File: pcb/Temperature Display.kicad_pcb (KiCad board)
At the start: 2 copper layers, 25.7 x 34.4 mm, 18 parts, among them P1 Connector_Generic:Conn_01x08, P2 Connector_Generic:Conn_01x08

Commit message: PCB cleanup / optimization and silkscreen adjustments
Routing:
- net /+3.3V: track 6.13 -> 0.00 mm
- net D2: vias 2 -> 0
- added copper zone on B.Cu, net /+3.3V
- added copper zone on F.Cu, net /GND
- removed copper zone on F.Cu, net /+3.3V
- removed copper zone on B.Cu, net /GND
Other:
- board text added: "GXHT30"
- board text added: "Rev 1.0"
- board text added: "SSD1306"
- board text added: "https://riii.me/td1"
- board text removed: "G"

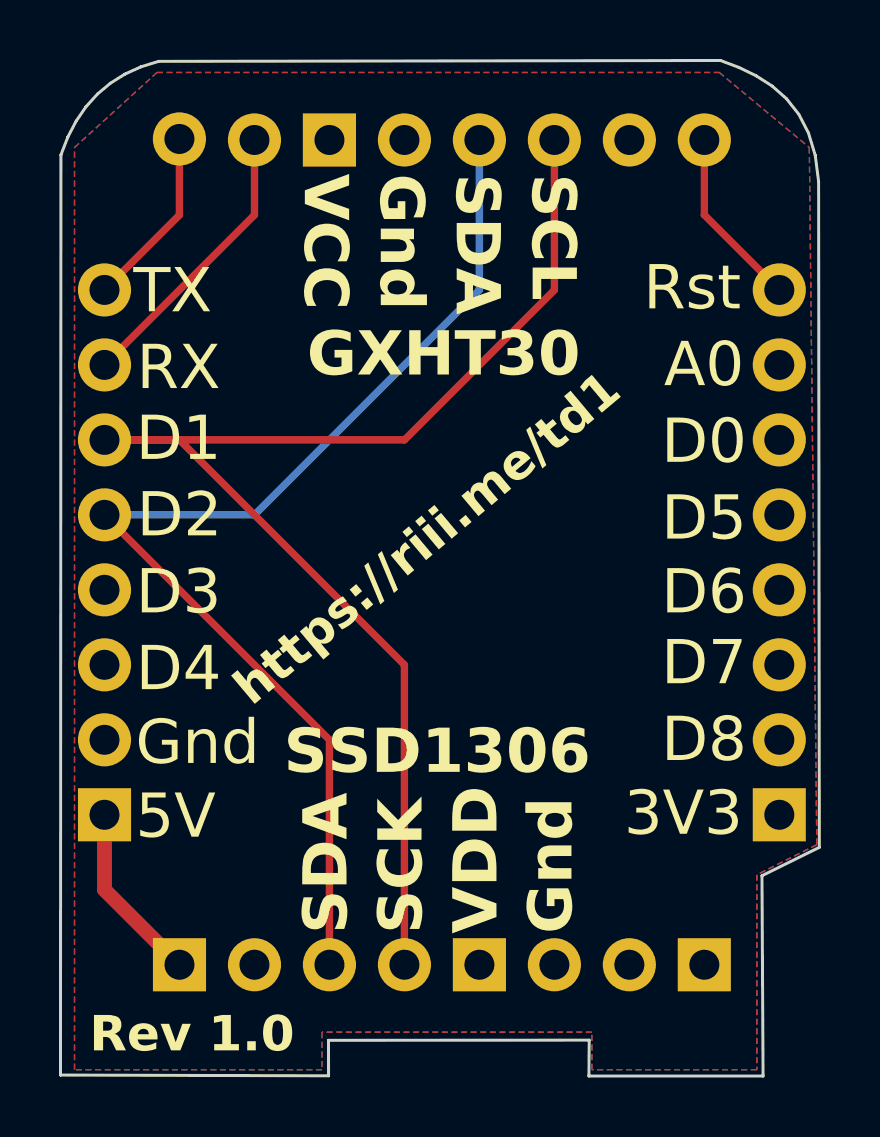
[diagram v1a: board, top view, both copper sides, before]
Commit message: More PCB optimization, minor README fixes
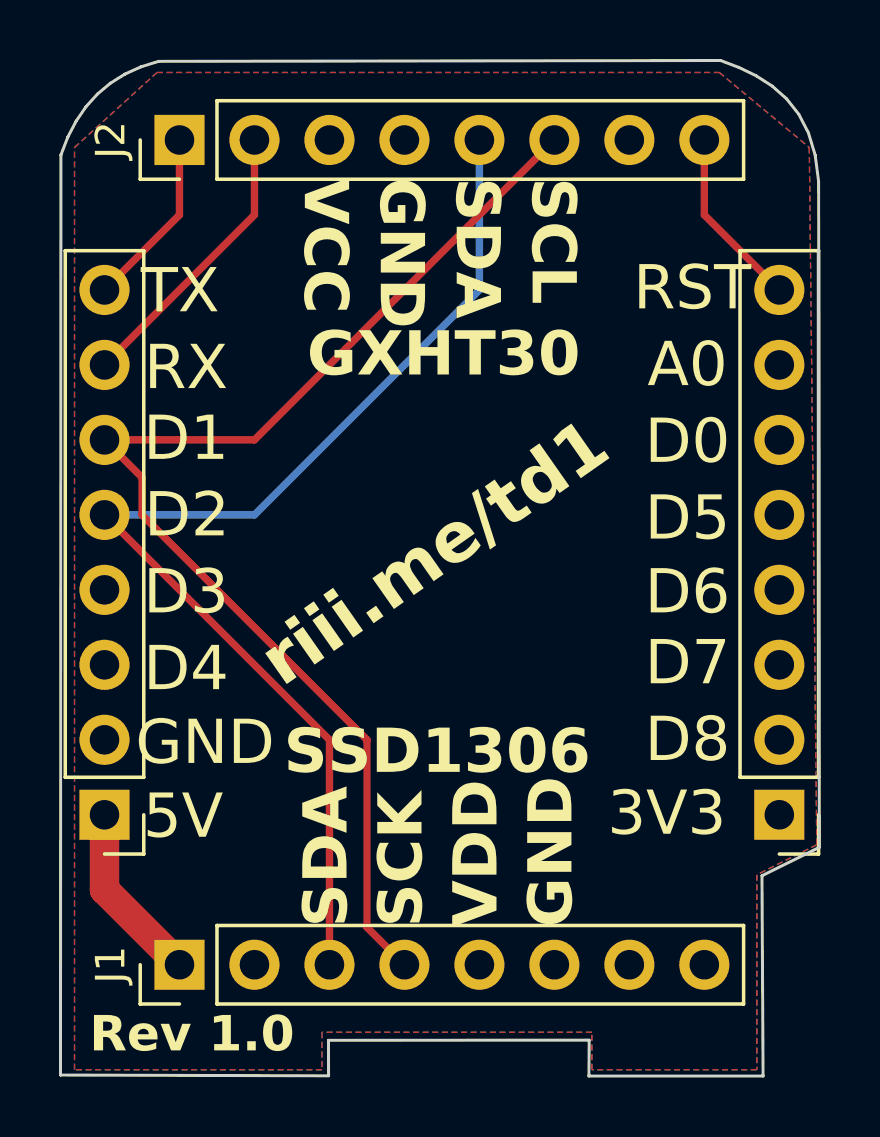
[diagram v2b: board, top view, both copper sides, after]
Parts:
- removed ? (x8), Gnd (x2), SCK, SCL, SDA (x2), VCC, VDD: , 
- added J1: SSD1306, Connector_PinHeader_2.54mm:PinHeader_1x08_P2.54mm_Vertical, F.Cu at (130.0, 109.0)
- added J2: GXHT30, Connector_PinHeader_2.54mm:PinHeader_1x08_P2.54mm_Vertical, F.Cu at (130.0, 81.1)
- P1, P2: footprint D1_mini:D1_mini_Pin_Header -> Connector_PinHeader_2.54mm:PinHeader_1x08_P2.54mm_Vertical
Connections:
- P1 pad 5: D2 -> /D2
- P1 pad 6: D1 -> /D1
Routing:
- net D1: track 45.9 -> 0.00 mm
- net /D1: track 0.00 -> 41.4 mm
- net D2: track 39.3 -> 0.00 mm
- net /D2: track 0.00 -> 39.3 mm
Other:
- board text added: "GND"
- board text added: "RST"
- board text added: "riii.me/td1"
- board text removed: "Gnd"
- board text removed: "Rst"
- board text removed: "https://riii.me/td1"
